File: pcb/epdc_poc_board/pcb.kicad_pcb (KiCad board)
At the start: 2 copper layers, 50 x 50 mm, 191 parts, among them J201 Conn_02x05_Odd_Even, J202 USB_C_Receptacle_USB2.0, J301 AXE550127, J302 FH26W-39S-0.3SHW, J601 DB15_Female_HighDensity_Mount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, J602 Conn_01x15_MountingPin, U104 XC6206PxxxMR, U201 ECP5U_45_CABGA256, U202 W25Q128JVP, U203 XC6206PxxxMR, U204 SY8008, U205 SY8008, U206 SY8008, U301 LM358, U302 LT1945, U303 LT3471, U502 MT41K256M16HA, U601 AD9984KCPZ, Y201 24MHz

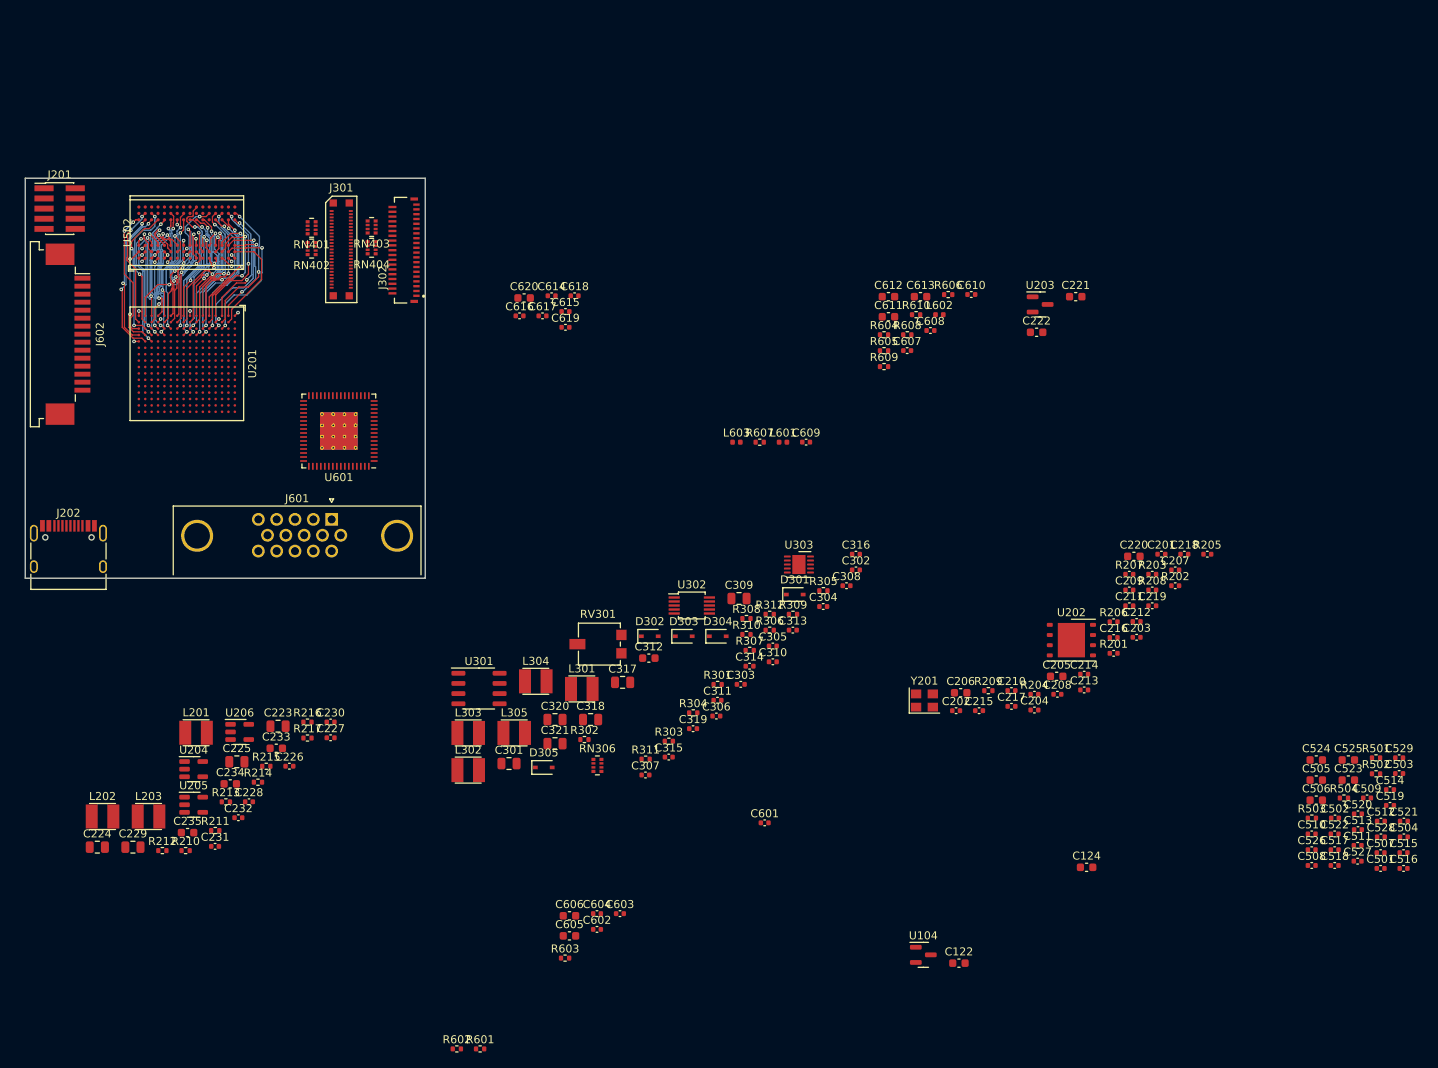
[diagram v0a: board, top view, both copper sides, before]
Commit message: - wip epdc poc board, going to remove vga input
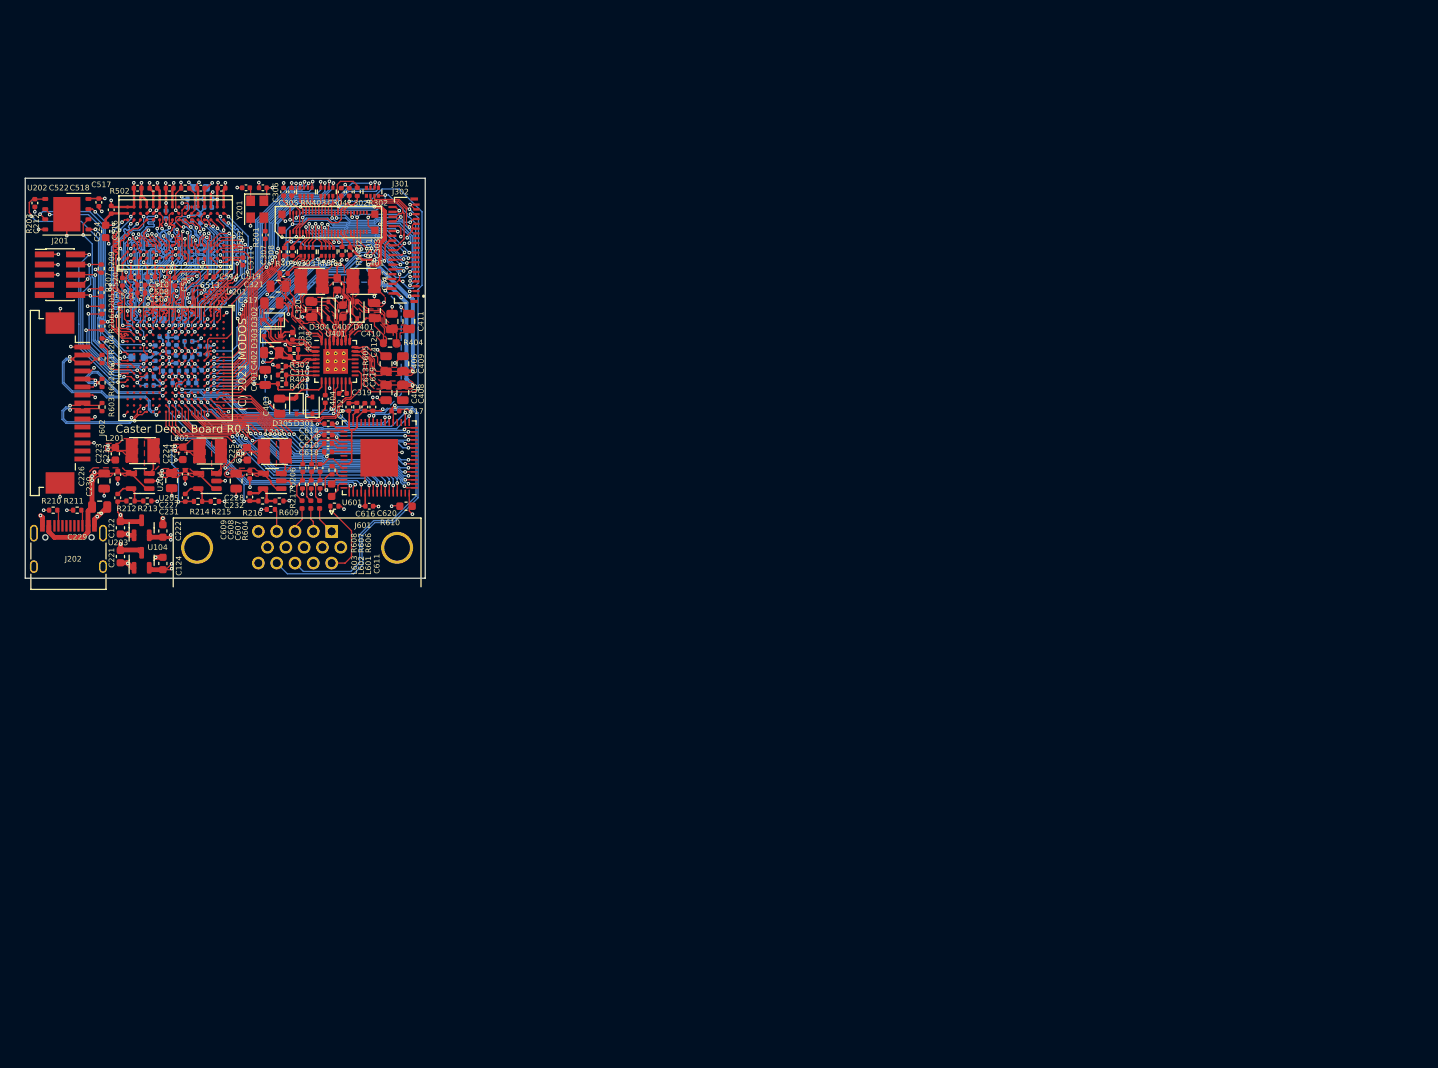
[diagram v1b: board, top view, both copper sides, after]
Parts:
- removed C205, C206, C505, C506, C605, C606: 22uF, Capacitor_SMD:C_0603_1608Metric
- removed C207, C208, C216, C218, C501, C504: 220nF, Capacitor_SMD:C_0402_1005Metric
- removed C301, C309, C318: 4.7uF/25V, Capacitor_SMD:C_0805_2012Metric
- removed C311, C316: 100pF, Capacitor_SMD:C_0402_1005Metric
- removed C314: 1uF, Capacitor_SMD:C_0402_1005Metric
- removed C315: 4.7pF, Capacitor_SMD:C_0402_1005Metric
- removed L301, L302: 22uH, footprints:L_1212
- removed L304: 10uH, footprints:L_1212
- removed L305: 15uH, footprints:L_1212
- removed R208: 10K, Capacitor_SMD:C_0402_1005Metric
- removed R303: DNP, Resistor_SMD:R_0402_1005Metric
- removed R304: 390K, Resistor_SMD:R_0402_1005Metric
- removed R305: 383K/1%, Resistor_SMD:R_0402_1005Metric
- removed R306: 27K/1%, Resistor_SMD:R_0402_1005Metric
- removed R309: 560K/1%, Resistor_SMD:R_0402_1005Metric
- removed R310: 36.5K/1%, Resistor_SMD:R_0402_1005Metric
- removed R311: 226K/1%, Resistor_SMD:R_0402_1005Metric
- removed R312: 15K/1%, Resistor_SMD:R_0402_1005Metric
- removed RV301: 200K, Potentiometer_SMD:Potentiometer_Vishay_TS53YL_Vertical
- removed U301: LM358, Package_SO:SO-8_3.9x4.9mm_P1.27mm
- removed U302: LT1945, Package_SO:MSOP-10_3x3mm_P0.5mm
- removed U303: LT3471, Package_DFN_QFN:DFN-10-1EP_3x3mm_P0.5mm_EP1.65x2.38mm
- added C401: 1uF/25V, Capacitor_SMD:C_0805_2012Metric, F.Cu at (130.0, 74.9)
- added C402: 1uF/25V, Capacitor_SMD:C_0805_2012Metric, F.Cu at (130.8, 71.8)
- added C403: 1uF/25V, Capacitor_SMD:C_0805_2012Metric, F.Cu at (131.8, 78.5)
- added C404: 100nF, Capacitor_SMD:C_0402_1005Metric, F.Cu at (137.5, 77.6)
- added C405: 4.7uF/25V, Capacitor_SMD:C_0805_2012Metric, F.Cu at (145.1, 76.8)
- added C406: 4.7uF/25V, Capacitor_SMD:C_0805_2012Metric, F.Cu at (145.1, 73.2)
- added C407: 10uF, Capacitor_SMD:C_0603_1608Metric, F.Cu at (139.7, 66.6)
- added C408: 4.7uF/25V, Capacitor_SMD:C_0805_2012Metric, F.Cu at (147.2, 76.8)
- added C409: 4.7uF/25V, Capacitor_SMD:C_0805_2012Metric, F.Cu at (147.2, 73.2)
- added C410: 4.7uF/25V, Capacitor_SMD:C_0805_2012Metric, F.Cu at (143.7, 66.5)
- added C411: 4.7uF/25V, Capacitor_SMD:C_0805_2012Metric, F.Cu at (147.9, 67.9)
- added C412: 4.7uF/25V, Capacitor_SMD:C_0805_2012Metric, F.Cu at (145.8, 67.9)
- added D401: B0530WS, Diode_SMD:D_SOD-323, F.Cu at (141.5, 66.5)
- added L401: 4.7uH, footprints:L_1212, F.Cu at (142.3, 62.9)
- added R401: 806K/1%, Resistor_SMD:R_0402_1005Metric, F.Cu at (132.1, 75.7)
- added R402: 49.9K/1%, Resistor_SMD:R_0402_1005Metric, F.Cu at (132.1, 74.6)
- added R403: 10R, Resistor_SMD:R_0402_1005Metric, F.Cu at (132.3, 61.9)
- added R404: 0.5R, Resistor_SMD:R_0603_1608Metric, F.Cu at (145.6, 70.6)
- added U401: MAX17135, Package_DFN_QFN:QFN-32-1EP_5x5mm_P0.5mm_EP3.1x3.1mm_ThermalVias, F.Cu at (138.8, 72.9)
- C201, C202, C203, C204, C210, C211, C213, C214, C215, C217, C219, C220, C502, C503, C509, C515, C523, C525, C526, C527, C528, C529, C601, C602, C603, C604, R501, R503, R504: moved to B.Cu
- C317: value 4.7uF/25V -> 1uF/25V
- C319: value 75pF -> 2.2nF
- C321: value 4.7uF/25V -> 1uF
- C612, C613: footprint Capacitor_SMD:C_0603_1608Metric -> Capacitor_SMD:C_0402_1005Metric
- L303: value 2.2uH -> 4.7uH
- R307: value 560K/1% -> 332K/1%
- U601: footprint Package_DFN_QFN:QFN-64-1EP_9x9mm_P0.5mm_EP4.7x4.7mm_ThermalVias -> Package_DFN_QFN:QFN-64-1EP_9x9mm_P0.5mm_EP4.7x4.7mm
- moved C516 181.3 mm to (110.8, 54.0), turned to 90 degrees
- moved C515 174.0 mm to (117.6, 54.5), turned to 90 degrees
- moved C521 172.6 mm to (113.7, 62.4), turned to 180 degrees
- moved C518 170.2 mm to (116.0, 51.2)
- moved C522 170.0 mm to (114.0, 51.2), turned to 180 degrees
- moved C507 170.0 mm to (114.5, 64.3), turned to 180 degrees
- moved C520 168.2 mm to (112.2, 63.0), turned to -90 degrees
- moved C517 167.5 mm to (118.0, 51.2), turned to 180 degrees
- moved C527 167.1 mm to (120.8, 53.6), turned to 180 degrees
- moved C514 166.6 mm to (122.0, 51.2), turned to 180 degrees
- moved R502 165.9 mm to (120.0, 51.2), turned to 180 degrees
- moved C519 165.2 mm to (124.5, 51.2)
- moved C512 165.1 mm to (118.7, 63.0), turned to -90 degrees
- moved C524 165.1 mm to (110.0, 56.6), turned to -90 degrees
- moved C508 163.3 mm to (114.5, 63.4), turned to 180 degrees
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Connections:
- C302 pad 1: /eink/BORDER -> VCOM
- C305 pad 1: +3V3_LCD -> +3V3
- C312 pad 1: GND -> GNDPWR
- C312 pad 2: +12V -> +5V
- C317 pad 1: GND -> Net-(C317-Pad1)
- C317 pad 2: VGH -> GNDPWR
- C319 pad 2: VNEG -> Net-(C319-Pad2)
- C320 pad 1: GND -> GNDPWR
- C320 pad 2: VNEG -> Net-(C320-Pad2)
- C321 pad 2: +12V -> Net-(C321-Pad2)
- C601 pad 1: +1V8 -> +3V3
- C603 pad 1: +1V8 -> +3V3
- C616 pad 1: +1V8 -> +3V3
- C617 pad 1: +1V8 -> +3V3
- D301 pad 1: VPOS -> Net-(C404-Pad1)
- D301 pad 2: Net-(D301-Pad2) -> VGL
- D302 pad 1: VGH -> Net-(C313-Pad1)
- D302 pad 2: Net-(D302-Pad2) -> Net-(C317-Pad1)
- D303 pad 1: GND -> VGH
- D303 pad 2: Net-(C313-Pad2) -> Net-(C313-Pad1)
- D304 pad 1: Net-(C313-Pad2) -> Net-(C320-Pad2)
- D304 pad 2: VGL -> Net-(D304-Pad2)
- D305 pad 1: GND -> Net-(C403-Pad2)
- D305 pad 2: Net-(C314-Pad2) -> Net-(C404-Pad1)
- J201 pad 10: unconnected-(J201-Pad10) -> /fpga/CRESET
- J301 pad 3: +3V3_LCD -> +3V3
- J301 pad 34: /eink/BORDER -> VCOM
- J301 pad 8: +3V3_LCD -> +3V3
- J302 pad 34: /eink/BORDER -> VCOM
- J302 pad 4: +3V3_LCD -> +3V3
- L303 pad 1: Net-(D301-Pad2) -> +5V
- L303 pad 2: +12V -> Net-(D304-Pad2)
- R301 pad 1: +3V3_LCD -> +3V3
- R307 pad 2: Net-(C315-Pad1) -> Net-(R307-Pad2)
- R308 pad 1: Net-(C315-Pad1) -> GND
- R308 pad 2: GND -> Net-(R307-Pad2)
- U201 pad A10: EPDC_D3 -> EPDC_D12
- U201 pad A11: EPDC_D10 -> EPDC_D14
- U201 pad A12: EPDC_D11 -> EPDC_SDOE
- U201 pad A13: EPDC_SDOE -> EPDC_SDCLK
- U201 pad A14: unconnected-(U201-PadA14) -> EPD_PWR_EN
- U201 pad A9: EPDC_D2 -> EPDC_D10
- U201 pad B10: EPDC_D4 -> EPDC_D11
- U201 pad B11: EPDC_D7 -> EPDC_D13
- U201 pad B12: EPDC_D12 -> EPDC_D15
- U201 pad B13: EPDC_D15 -> EPDC_SDLE
- U201 pad B14: unconnected-(U201-PadB14) -> EPD_VCOM_EN
- U201 pad B15: /fpga_vi/VGA_R1 -> /fpga_vi/VGA_G1
- U201 pad B16: /fpga_vi/VGA_R0 -> /fpga_vi/VGA_G3
- U201 pad B8: EPDC_GDSP -> EPDC_D8
- U201 pad B9: EPDC_SDCLK -> EPDC_D9
- U201 pad C10: EPDC_D5 -> EPDC_D3
- U201 pad C11: EPDC_D8 -> EPDC_D5
- U201 pad C12: EPDC_D13 -> EPDC_D7
- U201 pad C14: /fpga_vi/VGA_R2 -> /fpga_vi/VGA_G0
- U201 pad C15: /fpga_vi/VGA_R5 -> /fpga_vi/VGA_G2
- U201 pad C16: /fpga_vi/VGA_R4 -> /fpga_vi/VGA_G4
- U201 pad C9: EPDC_D0 -> EPDC_D1
- U201 pad D10: EPDC_D6 -> EPDC_D2
- U201 pad D11: EPDC_D9 -> EPDC_D4
- U201 pad D12: EPDC_D14 -> EPDC_D6
- U201 pad D13: EPDC_SDLE -> EPDC_GDSP
- U201 pad D14: /fpga_vi/VGA_R3 -> /fpga_vi/VGA_B3
- U201 pad D16: unconnected-(U201-PadD16) -> /fpga_vi/VGA_G5
- U201 pad D9: EPDC_D1 -> EPDC_D0
- U201 pad E14: /fpga_vi/VGA_R6 -> /fpga_vi/VGA_B4
- U201 pad E15: /fpga_vi/VGA_G0 -> /fpga_vi/VGA_G6
- U201 pad E16: /fpga_vi/VGA_G6 -> /fpga_vi/VGA_G7
- U201 pad F12: /fpga_vi/VGA_G2 -> unconnected-(U201-PadF12)
- U201 pad F13: /fpga_vi/VGA_G1 -> /fpga_vi/VGA_B1
- U201 pad F14: /fpga_vi/VGA_R7 -> /fpga_vi/VGA_B5
- U201 pad F15: /fpga_vi/VGA_G5 -> /fpga_vi/VGA_R0
- U201 pad F16: /fpga_vi/VGA_G7 -> /fpga_vi/VGA_R1
- U201 pad G12: /fpga_vi/VGA_G3 -> unconnected-(U201-PadG12)
- U201 pad G13: /fpga_vi/VGA_G4 -> /fpga_vi/VGA_B0
- U201 pad G14: /fpga_vi/VGA_B0 -> /fpga_vi/VGA_B6
- U201 pad G15: unconnected-(U201-PadG15) -> /fpga_vi/VGA_R2
- U201 pad G16: /fpga_vi/VGA_B6 -> /fpga_vi/VGA_R3
- U201 pad H11: +1V8 -> +3V3
- U201 pad H12: /fpga_vi/VGA_B2 -> EPD_PWR_SCL
- U201 pad H13: /fpga_vi/VGA_B3 -> /fpga_vi/VGA_B2
- U201 pad H14: /fpga_vi/VGA_B1 -> /fpga_vi/VGA_B7
- U201 pad H15: /fpga_vi/VGA_B7 -> /fpga_vi/VGA_R4
- U201 pad J11: +1V8 -> +3V3
- U201 pad J12: /fpga_vi/VGA_B5 -> unconnected-(U201-PadJ12)
- U201 pad J13: /fpga_vi/VGA_B4 -> EPD_PWR_SDA
- U201 pad J15: /fpga_vi/VGA_VS -> /fpga_vi/VGA_R5
- U201 pad J16: /fpga_vi/VGA_HS -> /fpga_vi/VGA_R6
- U201 pad K14: unconnected-(U201-PadK14) -> /fpga_vi/VGA_HS
- U201 pad K15: /fpga_vi/VGA_SCL -> /fpga_vi/VGA_R7
- U201 pad K16: /fpga_vi/VGA_SDA -> /fpga_vi/VGA_VS
- U204 pad 1: /power/EXTEN -> +5V
- U205 pad 1: /power/EXTEN -> +5V
- U206 pad 1: /power/EXTEN -> +5V
- U601 pad 21: +1V8 -> +3V3
- U601 pad 22: /fpga_vi/VGA_SDA -> EPD_PWR_SDA
- U601 pad 23: /fpga_vi/VGA_SCL -> EPD_PWR_SCL
- U601 pad 53: +1V8 -> +3V3
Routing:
- net GND: track 10.5 -> 203.3 mm, vias 14 -> 137
- net VCOM: track 0.00 -> 69.0 mm, vias 0 -> 3
- net EPDC_SDCE0: track 0.00 -> 60.5 mm, vias 0 -> 3
- net +1V35: track 7.25 -> 66.7 mm, vias 8 -> 23
- net +5V: track 0.00 -> 59.2 mm, vias 0 -> 8
- net VGH: track 0.00 -> 57.8 mm, vias 0 -> 5
- net VGL: track 0.00 -> 57.1 mm, vias 0 -> 8
- net +3V3: track 0.00 -> 50.1 mm, vias 0 -> 22
- net EPDC_GDSP: track 0.00 -> 49.9 mm, vias 0 -> 5
- net VPOS: track 0.00 -> 45.6 mm, vias 0 -> 5
- net Net-(J601-Pad14): track 0.00 -> 42.8 mm, vias 0 -> 1
- net EPDC_SDLE: track 0.00 -> 41.9 mm, vias 0 -> 2
- net EPDC_SDCLK: track 0.00 -> 41.2 mm, vias 0 -> 2
- net EPDC_GDCLK: track 0.00 -> 39.6 mm, vias 0 -> 4
- net EPDC_SDOE: track 0.00 -> 39.5 mm, vias 0 -> 2
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- added copper zone on F.Cu, net +1V1
- added copper zone on In1.Cu, net +1V1
- added copper zone on F.Cu, net +1V35
- added copper zone on In1.Cu, net +1V35
- added copper zone on In1.Cu, net +1V8
- added copper zone on In1.Cu, net +2V5
- added copper zone on F.Cu, net +3V3
- added copper zone on In1.Cu, net +3V3
- added copper zone on F.Cu, net +5V
- added copper zone on In1.Cu, net +5V
- added copper zone on In2.Cu, net GND
- added copper zone on B.Cu, net GNDPWR
- added copper zone on F.Cu, net GNDPWR
- added copper zone on F.Cu, net Net-(C313-Pad1)
- added copper zone on F.Cu, net Net-(C317-Pad1)
- added copper zone on F.Cu, net Net-(C320-Pad2)
- added copper zone on F.Cu, net Net-(C321-Pad2)
- added copper zone on F.Cu, net Net-(C410-Pad2)
- added copper zone on F.Cu, net Net-(C411-Pad2)
- added copper zone on F.Cu, net Net-(D304-Pad2)
- added copper zone on F.Cu, net Net-(D401-Pad1)
- added copper zone on F.Cu, net Net-(L201-Pad1)
- added copper zone on F.Cu, net Net-(L202-Pad1)
- added copper zone on F.Cu, net Net-(L203-Pad1)
- added copper zone on F.Cu, net VGH
- added copper zone on F.Cu, net VNEG
- added copper zone on F.Cu, net VPOS
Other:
- copper layers 2 -> 4
- board text added: "(C) 2021 MODOS"
- board text added: "Caster Demo Board R0.1"

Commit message: pcb: switch to s6 for epdc board
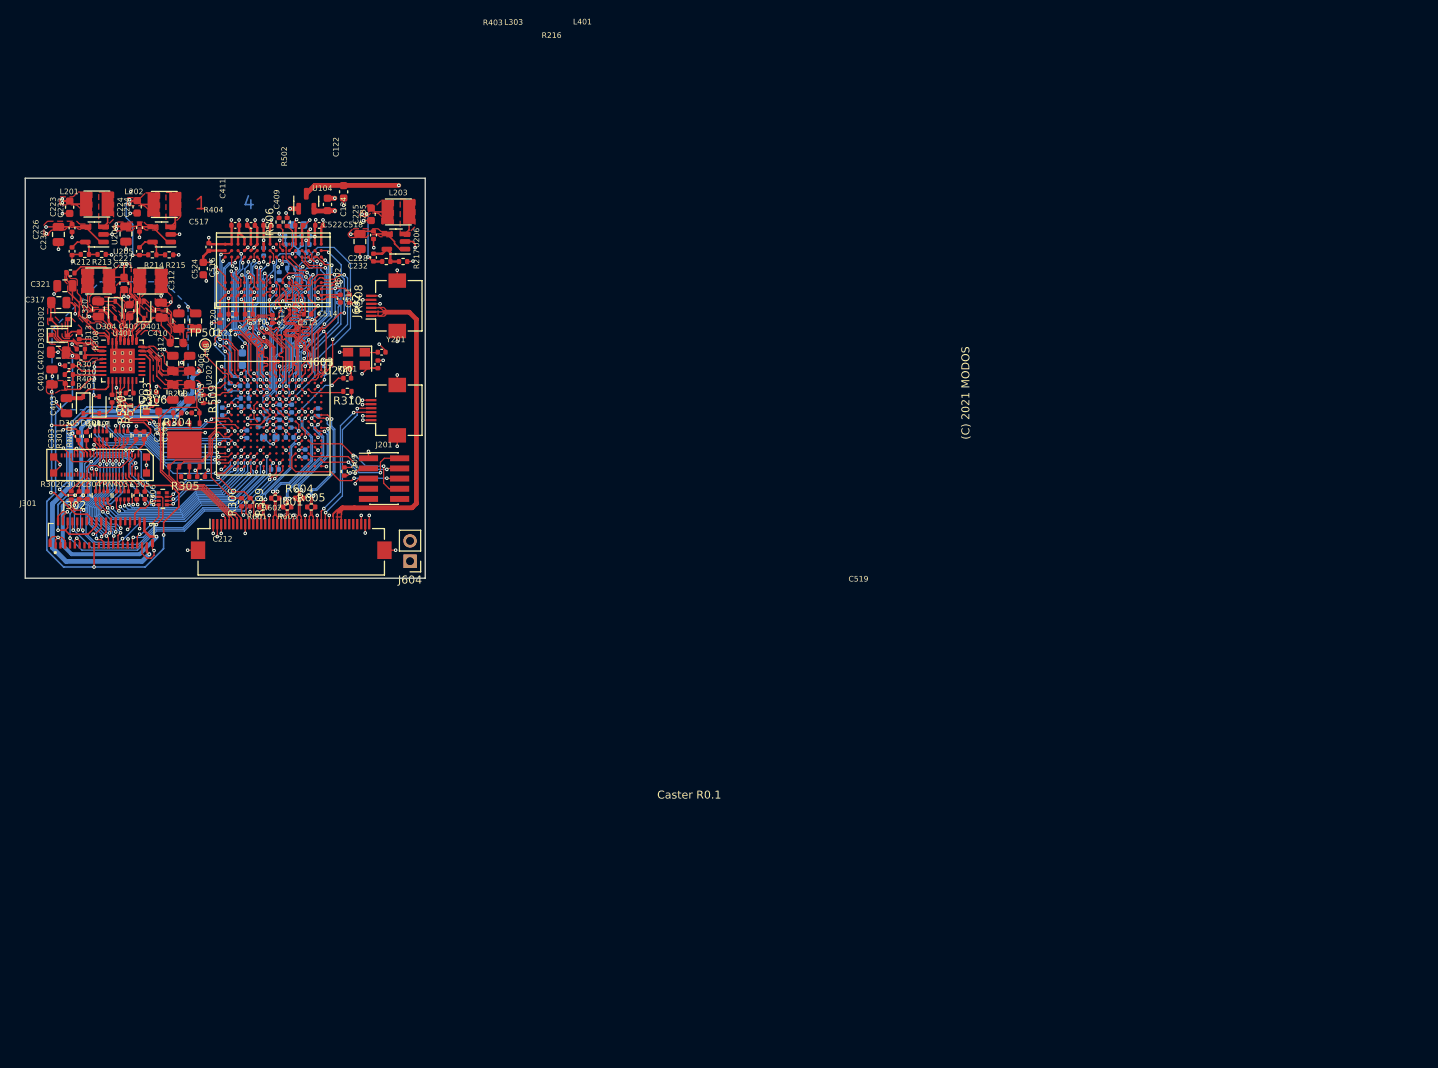
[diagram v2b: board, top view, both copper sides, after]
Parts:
- removed C221, C222, C611: 10uF, Capacitor_SMD:C_0603_1608Metric
- removed C229: 10uF/25V, Capacitor_SMD:C_0805_2012Metric
- removed C507, C528: 10nF, Capacitor_SMD:C_0402_1005Metric
- removed C601, C602, C603, C604, C614, C615, C616, C617, C618, C619: 220nF, Capacitor_SMD:C_0402_1005Metric
- removed C607, C608, C609: 47nF, Capacitor_SMD:C_0402_1005Metric
- removed C610: 1nF, Capacitor_SMD:C_0402_1005Metric
- removed C612: 82nF, Capacitor_SMD:C_0402_1005Metric
- removed C613: 8.2nF, Capacitor_SMD:C_0402_1005Metric
- removed C620: 22uF, Capacitor_SMD:C_0603_1608Metric
- removed J202: USB_C_Receptacle_USB2.0, Connector_USB:USB_C_Receptacle_HRO_TYPE-C-31-M-12
- removed L601, L602, L603: 220, Inductor_SMD:L_0402_1005Metric
- removed R204, R205, R206, R207: 10K, Capacitor_SMD:C_0402_1005Metric
- removed R210, R211: 5.1K, Resistor_SMD:R_0402_1005Metric
- removed R606, R607, R608: 75, Resistor_SMD:R_0402_1005Metric
- removed R609, R610: 0, Resistor_SMD:R_0402_1005Metric
- removed U201: ECP5U_45_CABGA256, Package_BGA:BGA-256_14.0x14.0mm_Layout16x16_P0.8mm_Ball0.45mm_Pad0.32mm_NSMD
- removed U203: XC6206PxxxMR, Package_TO_SOT_SMD:SOT-23
- removed U601: AD9984KCPZ, Package_DFN_QFN:QFN-64-1EP_9x9mm_P0.5mm_EP4.7x4.7mm
- added C501: 220nF, Capacitor_SMD:C_0402_1005Metric, B.Cu at (127.7, 82.0)
- added C504: 220nF, Capacitor_SMD:C_0402_1005Metric, B.Cu at (127.3, 76.0)
- added D306: LED, LED_SMD:LED_0603_1608Metric, F.Cu at (115.9, 79.1)
- added J603: Conn_01x06_MountingPin, Connector_FFC-FPC:Hirose_FH12-6S-0.5SH_1x06-1MP_P0.50mm_Horizontal, F.Cu at (145.1, 79.0)
- added J604: Conn_01x02, Connector_PinHeader_2.54mm:PinHeader_1x02_P2.54mm_Vertical, F.Cu at (148.1, 97.9)
- added R303: 1K, Resistor_SMD:R_0402_1005Metric, F.Cu at (116.4, 77.3)
- added R304: 4.7K, Resistor_SMD:R_0402_1005Metric, F.Cu at (119.0, 79.3)
- added R305: 4.7K, Resistor_SMD:R_0402_1005Metric, F.Cu at (120.0, 87.3)
- added R306: 4.7K, Resistor_SMD:R_0402_1005Metric, F.Cu at (127.0, 90.5)
- added R309: 4.7K, Resistor_SMD:R_0402_1005Metric, F.Cu at (128.1, 90.5)
- added R310: 4.7K, Resistor_SMD:R_0402_1005Metric, F.Cu at (140.3, 76.7)
- added R505: 100R 1%, Resistor_SMD:R_0402_1005Metric, B.Cu at (127.4, 77.5)
- added R506: 4.7K, Resistor_SMD:R_0402_1005Metric, F.Cu at (131.7, 55.5)
- added R507: 4.7K, Resistor_SMD:R_0402_1005Metric, B.Cu at (131.8, 62.2)
- added R508: 4.7K, Resistor_SMD:R_0402_1005Metric, F.Cu at (140.5, 65.1)
- added R509: 4.7K, Resistor_SMD:R_0402_1005Metric, F.Cu at (122.2, 77.6)
- added R510: 4.7K, Resistor_SMD:R_0402_1005Metric, F.Cu at (113.2, 78.9)
- added R511: 4.7K, Resistor_SMD:R_0402_1005Metric, F.Cu at (111.8, 79.0)
- added TP501: TestPoint, TestPoint:TestPoint_Pad_D1.0mm, F.Cu at (122.5, 70.8)
- added U200: XC6SLX16-FTG256, Package_BGA:BGA-256_14.0x14.0mm_Layout16x16_P0.8mm_Ball0.45mm_Pad0.32mm_NSMD, F.Cu at (131.0, 80.0)
- C508: moved to B.Cu
- J302: value FH26W-39S-0.3SHW -> 10064555-392120HLF; footprint footprints:HRS_FH26W-39S-0.3SHW(60) -> footprints:FCI_10064555-392120HLF
- J601: value DB15_Female_HighDensity_MountingHoles -> Conn_01x40_MountingPin; footprint Connector_Dsub:DSUB-15-HD_Female_Horizontal_P2.29x1.98mm_EdgePinOffset3.03mm_Housed_MountingHolesOffset4.94mm -> Connector_FFC-FPC:Hirose_FH12-40S-0.5SH_1x40-1MP_P0.50mm_Horizontal
- J602: value Conn_01x15_MountingPin -> Conn_01x06_MountingPin; footprint Connector_FFC-FPC:TE_1-84952-5_1x15-1MP_P1.0mm_Horizontal -> Connector_FFC-FPC:Hirose_FH12-6S-0.5SH_1x06-1MP_P0.50mm_Horizontal
- R307: value 332K/1% -> 562K/1%
- R604: value 10K -> 100
- R605: value 1.5K -> 100
- U202: value W25Q128JVP -> W25X16JVP
- moved R302 52.1 mm to (105.8, 89.7), turned to 90 degrees
- moved J302 52.0 mm to (109.5, 94.5), turned to 0 degrees
- moved C302 50.8 mm to (106.8, 89.6), turned to -90 degrees
- moved C122 50.4 mm to (139.8, 51.7)
- moved C304 49.4 mm to (107.8, 89.6), turned to -90 degrees
- moved U104 49.4 mm to (135.1, 52.9)
- moved C124 49.4 mm to (137.8, 53.3)
- moved J201 47.9 mm to (144.8, 87.5)
- moved RN404 47.3 mm to (109.5, 89.7), turned to 90 degrees
- moved RN306 46.5 mm to (117.2, 90.1), turned to 0 degrees
- moved RN403 44.3 mm to (112.2, 89.7), turned to 90 degrees
- moved C305 42.6 mm to (113.9, 89.7), turned to -90 degrees
- moved C306 41.7 mm to (115.0, 89.7), turned to -90 degrees
- moved J301 41.7 mm to (109.3, 85.8), turned to 180 degrees
- moved J602 41.6 mm to (145.1, 66.0), turned to 90 degrees
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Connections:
- C201 pad 1: +3V3 -> +2V5
- C203 pad 1: +3V3 -> +2V5
- C209 pad 2: +3V3 -> +2V5
- C503 pad 1: +1V35 -> +3V3
- J601 pad 1: Net-(J601-Pad1) -> +5V
- J601 pad 10: GND -> FPGA_PROG
- J601 pad 11: Net-(J601-Pad11) -> FPGA_SUSP
- J601 pad 12: unconnected-(J601-Pad12) -> GND
- J601 pad 13: Net-(J601-Pad13) -> DSI_IN_D0P
- J601 pad 14: Net-(J601-Pad14) -> DSI_IN_D0N
- J601 pad 15: unconnected-(J601-Pad15) -> GND
- J601 pad 2: Net-(J601-Pad2) -> +5V
- J601 pad 3: Net-(J601-Pad3) -> +5V
- J601 pad 4: Net-(J601-Pad4) -> GND
- J601 pad 5: GND -> FPGA_FCS
- J601 pad 6: GND -> FPGA_FMISO
- J601 pad 7: GND -> FPGA_FMOSI
- J601 pad 8: GND -> FPGA_FCCLK
- J601 pad 9: unconnected-(J601-Pad9) -> GND
- J602 pad 1: GND -> /fpga_vi/TL_LED
- J602 pad 2: /fpga_vi/DSI_IN_D1N -> /fpga_vi/TL_LED
- J602 pad 3: /fpga_vi/DSI_IN_D1P -> /fpga_vi/TL_LED
- J602 pad 5: /fpga_vi/DSI_IN_CN -> GND
- J602 pad 6: /fpga_vi/DSI_IN_CP -> GND
- R201 pad 1: Net-(R201-Pad1) -> /fpga/GCLK
- R202 pad 1: +3V3 -> +2V5
- R203 pad 2: QSPI_A_SS0 -> FPGA_FCS
- R501 pad 1: /fpga_ddr/DRAM_CKP -> /fpga_ddr/DRAM_CKN
- R501 pad 2: /fpga_ddr/DRAM_CKN -> /fpga_ddr/DRAM_CKP
- R601 pad 1: /fpga_vi/DSI_IN_D1P -> DSI_IN_D0P
- R601 pad 2: /fpga_vi/DSI_IN_D1N -> DSI_IN_D0N
- R602 pad 1: /fpga_vi/DSI_IN_CP -> DSI_IN_D1P
- R602 pad 2: /fpga_vi/DSI_IN_CN -> DSI_IN_D1N
- R603 pad 1: /fpga_vi/DSI_IN_D0P -> DSI_IN_CP
- R603 pad 2: /fpga_vi/DSI_IN_D0N -> DSI_IN_CN
- R604 pad 1: GND -> DSI_IN_D2P
- R604 pad 2: Net-(R604-Pad2) -> DSI_IN_D2N
- R605 pad 1: Net-(C612-Pad1) -> DSI_IN_D3P
- R605 pad 2: Net-(C613-Pad1) -> DSI_IN_D3N
- U202 pad 1: QSPI_A_SS0 -> FPGA_FCS
- U202 pad 2: QSPI_A_DATA1 -> FPGA_FMISO
- U202 pad 3: QSPI_A_DATA2 -> Net-(R304-Pad1)
- U202 pad 5: QSPI_A_DATA0 -> FPGA_FMOSI
- U202 pad 6: QSPI_A_SCLK -> FPGA_FCCLK
- U202 pad 7: QSPI_A_DATA3 -> Net-(R305-Pad1)
- U401 pad 16: EPD_VCOM_EN -> unconnected-(U401-Pad16)
- U401 pad 18: EPD_PWR_EN -> unconnected-(U401-Pad18)
- U401 pad 5: EPD_PWR_OK -> unconnected-(U401-Pad5)
- Y201 pad 4: +3V3 -> +2V5
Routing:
- net /fpga_vi/TL_LED: track 0.00 -> 49.2 mm
- net Net-(J601-Pad14): track 42.8 -> 0.00 mm, vias 1 -> 0
- net Net-(J601-Pad13): track 38.6 -> 0.00 mm, vias 1 -> 0
- net QSPI_A_SS0: track 33.8 -> 0.00 mm, vias 2 -> 0
- net /fpga_vi/VGA_R5: track 32.4 -> 0.00 mm, vias 2 -> 0
- net /fpga_vi/VGA_R2: track 32.3 -> 0.00 mm, vias 2 -> 0
- net /fpga_vi/VGA_G6: track 32.2 -> 0.00 mm, vias 2 -> 0
- net /fpga_vi/VGA_B7: track 32.0 -> 0.00 mm, vias 2 -> 0
- net /fpga_vi/VGA_R7: track 32.0 -> 0.00 mm, vias 2 -> 0
- net /fpga_vi/VGA_R0: track 31.8 -> 0.00 mm, vias 2 -> 0
- net /fpga_vi/VGA_R4: track 31.7 -> 0.00 mm, vias 2 -> 0
- net FPGA_FCS: track 0.00 -> 31.6 mm
- net /fpga_vi/VGA_B2: track 31.5 -> 0.00 mm, vias 2 -> 0
- net /fpga_vi/VGA_B0: track 31.5 -> 0.00 mm, vias 2 -> 0
- net /fpga_vi/VGA_G7: track 31.5 -> 0.00 mm, vias 2 -> 0
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- added copper zone on F.Cu, net /fpga_vi/TL_LED
- added copper zone on F.Cu, net VGL
- removed copper zone on In1.Cu, net +1V8
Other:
- board text added: "Caster R0.1"
- board text removed: "Caster Demo Board R0.1"
